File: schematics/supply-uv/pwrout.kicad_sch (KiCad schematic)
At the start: 60 parts, among them Q10 STP13NK60Z, Q11 IRLML0030, Q7 IRLML0030, Q8 IRLML0030, Q9 STP13NK60Z, U14 EL817, U15 UC3525, U16 IRS21867S, U17 EL817, U18 INA169

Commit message: Board#1 schematics rewrited
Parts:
- added TP22: PWR_SHUTDOWN, Library:TestPoint_Plated_Hole_D1.0mm, symbol Connector:TestPoint
- added TP23: STB_GND, Library:TestPoint_Plated_Hole_D1.0mm, symbol Connector:TestPoint
- added TP24: HV_GND, Library:TestPoint_Plated_Hole_D1.0mm, symbol Connector:TestPoint
- added TP28: PWR_FEEDBACK, Library:TestPoint_Plated_Hole_D1.0mm, symbol Connector:TestPoint
- added TP29: PWR_VCC, Library:TestPoint_Plated_Hole_D1.0mm, symbol Connector:TestPoint
- added TP30: PWR_GND, Library:TestPoint_Plated_Hole_D1.0mm, symbol Connector:TestPoint
- NT2, NT3: footprint NetTie:NetTie-2_SMD_Pad2.0mm -> NetTie:NetTie-2_SMD_Pad0.5mm
- renumbered C48 to C47, C49 to C48, C47 to C49, CLR3 to CLR4, CLR4 to CLR5, CLR5 to CLR6, D13 to D15, D14 to D16, R44 to R42, R45 to R43, R42 to R44, R43 to R45, TP9 to TP20, TP10 to TP21, TP11 to TP25, TP12 to TP26, TP13 to TP27
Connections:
- net DCDC_FEEDBACK: now also TP28.1
- net DCDC_SHUTDOWN: now also TP22.1
- net HV_GND: now also U16.4 (COM), TP24.1
- net PWR_GND: now also TP30.1
- net PWR_VCC: now also TP29.1
- net STB_GND: now also TP23.1; no longer U16.4 (COM)
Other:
- moved on the sheet: C49, NT2, R44, R45

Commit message: added some protection logic
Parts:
- added C53, C61: 100 nF, Capacitor_SMD:C_0603_1608Metric, symbol Device:C
- added D19: SMBJ3.3A, Diode_SMD:D_SMB, symbol Diode:SMAJ400A
- added F5: 5A, Library:FuseHolder1808, symbol Device:Fuse
- added Q8: IRLML5203, Package_TO_SOT_SMD:SOT-23, symbol Transistor_FET:IRLML5203
- added R44: 220, Resistor_SMD:R_0805_2012Metric, symbol Device:R
- added R52: 10K, Resistor_SMD:R_0805_2012Metric, symbol Device:R
- added R53: 110K, Resistor_SMD:R_0805_2012Metric, symbol Device:R
- added R58: 0.04R, Resistor_SMD:R_2512_6332Metric, symbol Device:R
- added U17: ~, symbol My_Library:AD822
- renumbered C47 to C50, C48 to C51, C49 to C52, C50 to C54, C51 to C55, C52 to C56, C53 to C57, C54 to C58, C55 to C59, C56 to C60, C57 to C62, C58 to C63, C59 to C64, C60 to C65, C61 to C66, C62 to C67, C63 to C68, C64 to C69, D15 to D20, D16 to D21, Q9 to Q10, Q10 to Q11, Q11 to Q12, Q8 to Q9, R42 to R45, R43 to R46, R44 to R47, R45 to R48, R46 to R49, R47 to R50, R48 to R51, R49 to R54, R50 to R55, R51 to R56, R52 to R57, R53 to R59, R54 to R60, R55 to R61, R56 to R62, R57 to R63, R58 to R64, R59 to R65, U14 to U15, U15 to U16, U16 to U18, U17 to U19, U18 to U20
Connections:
- net DCDC_2V5_VREF: now also U17.6 (IN2-)
- net DCDC_5V_VREF: now also C61.1, Q8.2 (S), U17.8 (VCC); no longer U15.4
- net HV_GND: now also R58.1; no longer Q11.3 (S)
- net HV_VCC: now also F5.1; no longer C59.1, C60.2, C62.2, Q10.2 (D)
- net STB_GND: now also C53.2, C61.2, D19.2 (A2), R52.1, U17.4 (GND)
- net VSYS_PWR renamed VSYS_PWR_VCC
- new net: C53.1, D19.1 (A1), R44.2, U17.3 (IN1+)
- new net: R53.2, U17.1 (OUT1), U17.5 (IN2+)
- new net: Q8.3 (D), U15.4
- new net: R52.2, R53.1, U17.2 (IN1-)
- new net DCDC_CURRENT_SENSE: Q11.3 (S), R44.1, R58.2
- new net DCDC_OVERPOWER#: Q8.1 (G), U17.7 (OUT2)
- new net HV_VCC_FUSE: C59.1, C60.2, C62.2, F5.2, Q10.2 (D)
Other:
- moved on the sheet: C57, C60, C63, Q9, R54, R55, TP22

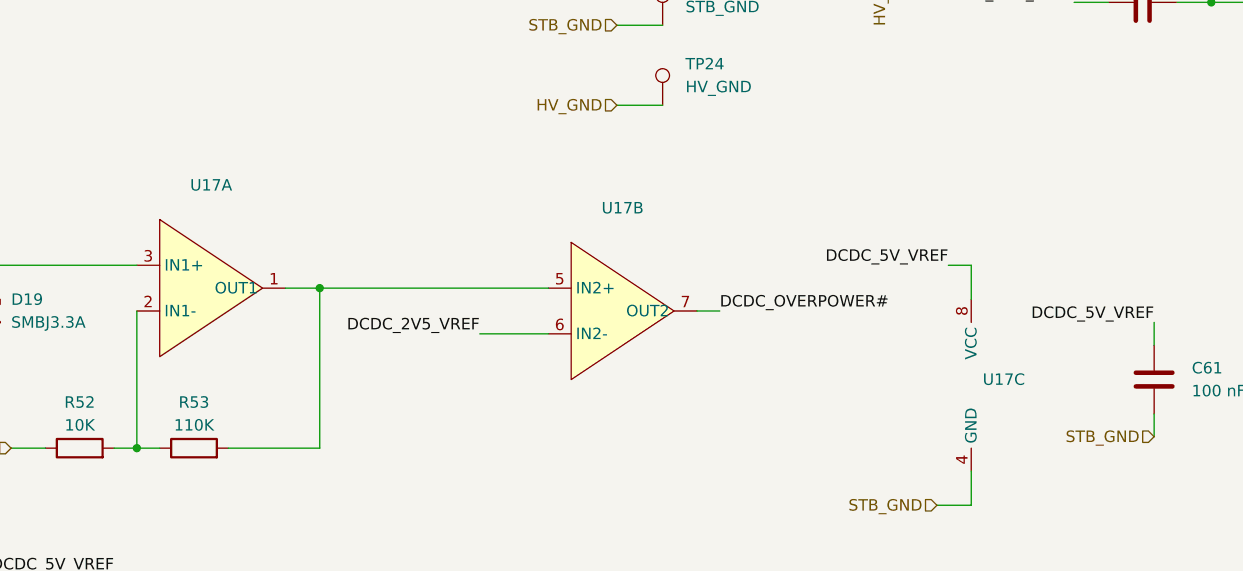
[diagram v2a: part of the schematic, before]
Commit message: changed operation amplifier
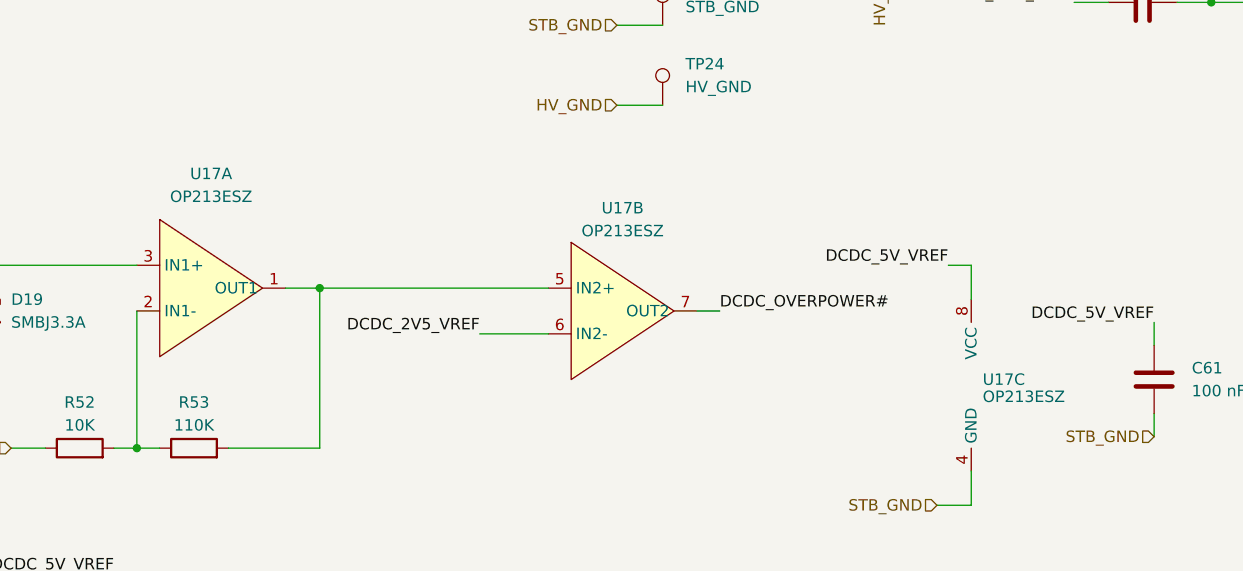
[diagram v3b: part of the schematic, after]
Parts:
- U17: value ~ -> OP213ESZ; footprint (none) -> Package_SO:SO-8_3.9x4.9mm_P1.27mm
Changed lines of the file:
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@@
 			)
 		)
-		(property "Value" "~"
+		(property "Value" "OP213ESZ"
 			(at 140.335 167.64 0)
 			(effects
@@
 			)
 		)
-		(property "Footprint" ""
+		(property "Footprint" "Package_SO:SO-8_3.9x4.9mm_P1.27mm"
 			(at 138.43 176.53 0)
 			(effects
@@
 			)
 		)
-		(property "Value" "~"
+		(property "Value" "OP213ESZ"
 			(at 180.34 186.055 0)
 			(effects
@@
 			)
 		)
-		(property "Footprint" ""
+		(property "Footprint" "Package_SO:SO-8_3.9x4.9mm_P1.27mm"
 			(at 179.07 184.15 0)
 			(effects
@@
 		(fields_autoplaced yes)
 		(property "Reference" "U17"
-			(at 94.615 162.56 0)
+			(at 94.615 161.29 0)
 			(effects
 				(font
@@
 			)
 		)
-		(property "Value" "~"
-			(at 94.615 165.1 0)
+		(property "Value" "OP213ESZ"
+			(at 94.615 163.83 0)
 			(effects
 				(font
@@
 			)
 		)
-		(property "Footprint" ""
+		(property "Footprint" "Package_SO:SO-8_3.9x4.9mm_P1.27mm"
 			(at 92.71 173.99 0)
 			(effects

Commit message: First board routing completed. I will review it few days later and maybe optimize something, but base worki done
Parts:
- removed D19: SMBJ3.3A, Diode_SMD:D_SMB, symbol Diode:SMAJ400A
- removed TP29: PWR_VCC, Library:TestPoint_Plated_Hole_D1.0mm, symbol Connector:TestPoint
- removed TP30: PWR_GND, Library:TestPoint_Plated_Hole_D1.0mm, symbol Connector:TestPoint
- added C59: 100 nF, Capacitor_SMD:C_0603_1608Metric, symbol Device:C
- added D19: SM6T30CA, Diode_SMD:D_SMB, symbol Device:D_TVS
- added JP7: Overpower mode, Connector_PinSocket_2.54mm:PinSocket_1x03_P2.54mm_Vertical, symbol Jumper:SolderJumper_3_Open
- TP20: renamed from TP22; footprint Library:TestPoint_Plated_Hole_D1.0mm -> TestPoint:TestPoint_Pad_1.0x1.0mm
- TP26: renamed from TP28; footprint Library:TestPoint_Plated_Hole_D1.0mm -> TestPoint:TestPoint_Pad_1.0x1.0mm
- renumbered C50 to C51, C51 to C52, C52 to C53, C53 to C54, C54 to C55, C55 to C56, C56 to C57, C57 to C58, C58 to C60, C59 to C61, C60 to C62, C61 to C63, C62 to C64, C63 to C65, C64 to C66, C65 to C67, C66 to C68, C67 to C69, C68 to C70, C69 to C71, R44 to R46, R45 to R47, R46 to R48, R47 to R49, R48 to R50, R49 to R51, R50 to R52, R51 to R53, R52 to R54, R53 to R55, R54 to R56, R55 to R57, R56 to R58, R57 to R59, R58 to R60, R59 to R61, R60 to R62, R61 to R63, R62 to R64, R63 to R65, R64 to R66, R65 to R67, TP20 to TP18, TP21 to TP19, TP23 to TP21, TP24 to TP22, TP25 to TP23, TP26 to TP24, TP27 to TP25
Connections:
- net DCDC_5V_VREF: now also JP7.1 (A); no longer C63.1, U17.8 (VCC)
- net HV_GND: now also C54.2, C63.2, R54.1, U17.4 (GND), D19.1 (A1)
- net STB_GND: now also C59.2; no longer C54.2, C63.2, R54.1, U17.4 (GND)
- net STB_VCC: now also C63.1, U17.8 (VCC), C59.1
- net at C54.1, R46.2, U17.3 (IN1+): now also D19.2 (A2)
- net at U15.4: now also JP7.2 (C); no longer Q8.3 (D)
- new net: JP7.3 (B), Q8.3 (D)
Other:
- moved on the sheet: C58, Q8

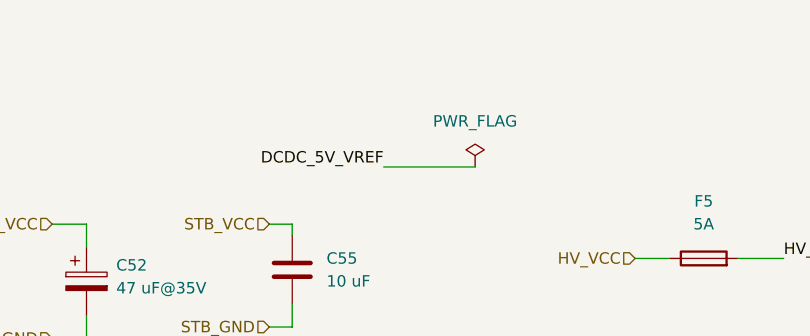
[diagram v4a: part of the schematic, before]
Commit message: first board routed
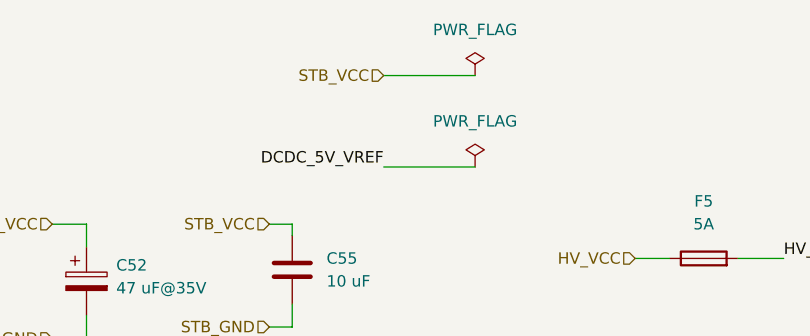
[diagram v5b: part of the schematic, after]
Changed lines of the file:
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@@
 	(wire
 		(pts
+			(xy 66.04 21.59) (xy 76.2 21.59)
+		)
+		(stroke
+			(width 0)
+			(type default)
+		)
+	)
+	(wire
+		(pts
 			(xy 205.74 100.33) (xy 205.74 101.6)
 		)
@@
 	(hierarchical_label "STB_VCC"
 		(shape input)
+		(at 66.04 21.59 180)
+		(fields_autoplaced yes)
+		(effects
+			(font
+				(size 1.27 1.27)
+			)
+			(justify right)
+		)
+	)
+	(hierarchical_label "STB_VCC"
+		(shape input)
 		(at 29.21 38.1 180)
 		(fields_autoplaced yes)
@@
 	)
 	(symbol
+		(lib_id "power:PWR_FLAG")
+		(at 76.2 21.59 0)
+		(unit 1)
+		(exclude_from_sim no)
+		(in_bom yes)
+		(on_board yes)
+		(dnp no)
+		(fields_autoplaced yes)
+		(property "Reference" "#FLG014"
+			(at 76.2 19.685 0)
+			(effects
+				(font
+					(size 1.27 1.27)
+				)
+				(hide yes)
+			)
+		)
+		(property "Value" "PWR_FLAG"
+			(at 76.2 16.51 0)
+			(effects
+				(font
+					(size 1.27 1.27)
+				)
+			)
+		)
+		(property "Footprint" ""
+			(at 76.2 21.59 0)
+			(effects
+				(font
+					(size 1.27 1.27)
+				)
+				(hide yes)
+			)
+		)
+		(property "Datasheet" "~"
+			(at 76.2 21.59 0)
+			(effects
+				(font
+					(size 1.27 1.27)
+				)
+				(hide yes)
+			)
+		)
+		(property "Description" "Special symbol for telling ERC where power comes from"
+			(at 76.2 21.59 0)
+			(effects
+				(font
+					(size 1.27 1.27)
+				)
+				(hide yes)
+			)
+		)
+		(pin "1"
+		)
+		(instances
+			(project "supply-uv"
+				(path "/ef40850c-d0bf-4cba-961b-9aba418f8e73/3be77773-a110-4db5-84df-23304730890a"
+					(reference "#FLG014")
+					(unit 1)
+				)
+			)
+		)
+	)
+	(symbol
 		(lib_id "Connector:TestPoint")
 		(at 251.46 233.68 0)
@@
 		(dnp no)
 		(fields_autoplaced yes)
-		(property "Reference" "#FLG013"
+		(property "Reference" "#FLG015"
 			(at 76.2 29.845 0)
 			(effects
@@
 			(project "supply-uv"
 				(path "/ef40850c-d0bf-4cba-961b-9aba418f8e73/3be77773-a110-4db5-84df-23304730890a"
-					(reference "#FLG013")
+					(reference "#FLG015")
 					(unit 1)
 				)
